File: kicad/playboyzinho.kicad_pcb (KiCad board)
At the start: 2 copper layers, 15 parts, among them SW1 SW_Push, SW2 SW_Push, SW3 SW_Push, SW4 SW_Push, SW5 SW_Push, SW6 SW_Push, SW7 SW_Push, SW8 SW_Push, SW9 SW_SPDT, U1 esp32-s3-pl, U7 (amplificador)_MAX98357_Module

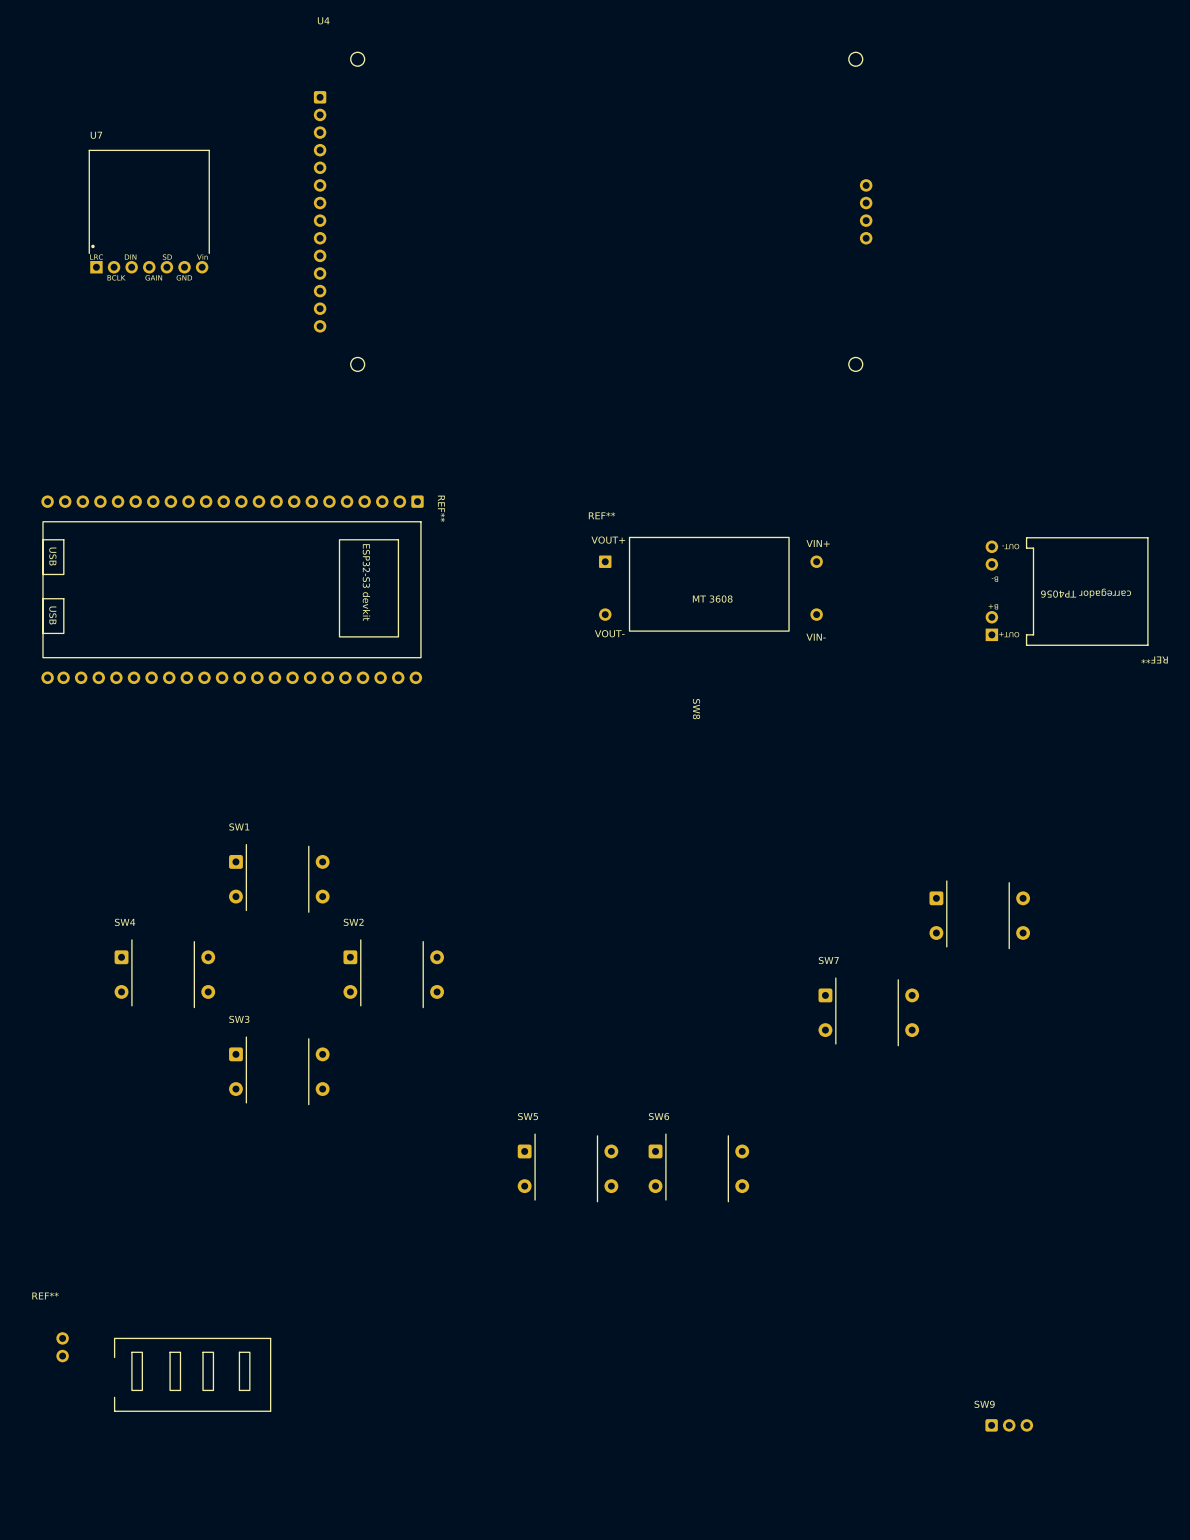
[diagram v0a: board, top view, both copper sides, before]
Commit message: fix: corrige conexões do esquemático e direção dos pinos de determinados símbolos
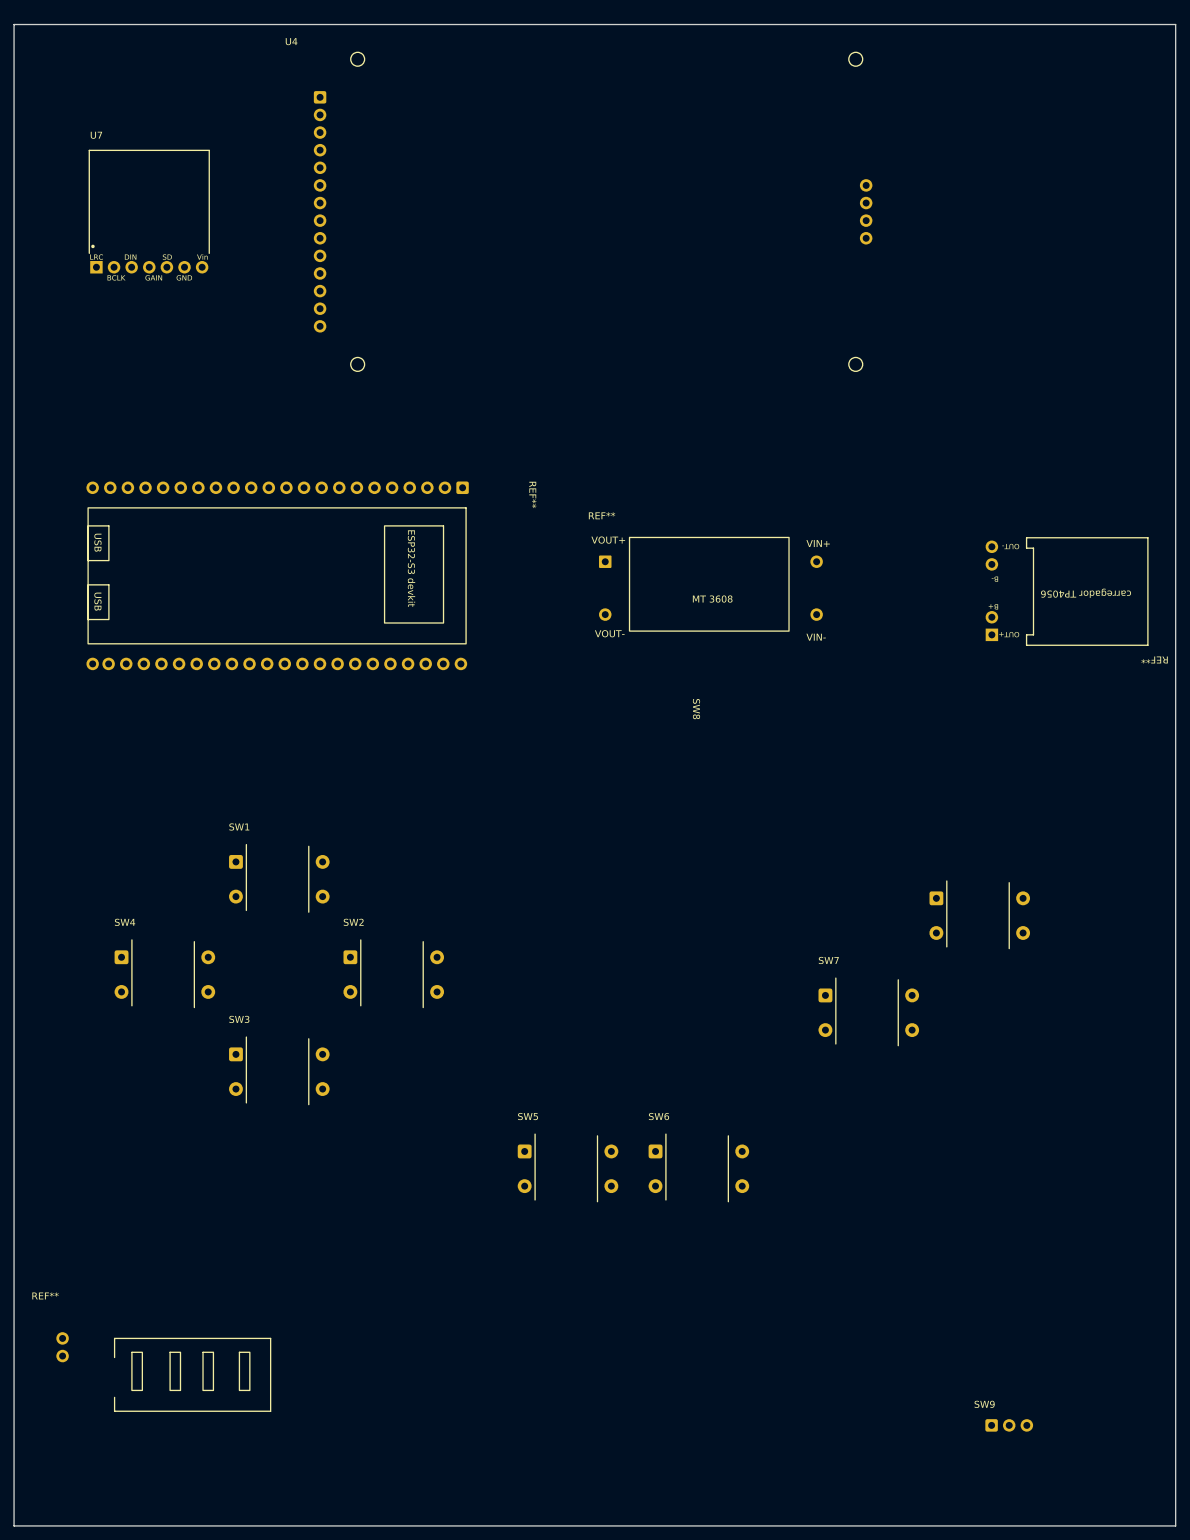
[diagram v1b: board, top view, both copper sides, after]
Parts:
- moved U1 6.80 mm to (-178.8, 40.3)
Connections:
- SW9 pad 1: +BATT -> unconnected-(SW9-A-Pad1)
- SW9 pad 2: -BATT -> Net-(SW9-B)
- SW9 pad 3: unconnected-(SW9-C-Pad3) -> Net-(SW9-C)
- U3 pad 3: +BATT -> Net-(SW9-C)
- U3 pad 4: GND -> Net-(U3-VIN-)
- U4 pad 18: /SD_CS -> /SCK
- U5 pad 1: +5V -> Net-(SW9-B)
- U5 pad 4: GND -> Net-(U3-VIN-)
- U6 pad 1: +BATT -> Net-(SW9-C)
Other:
- board outline added: 167.5 x 216.5 mm
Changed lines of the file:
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@@
 		)
 		(property "Value" "(amplificador)_MAX98357_Module"
-			(at 8.62 4.5 0)
+			(at 7 3.5 0)
 			(unlocked yes)
 			(layer "F.Fab")
@@
 	(footprint "lib-do-playboy:esp32-s3"
 		(layer "F.Cu")
-		(at -185.322001 42.3 -90)
+		(at -178.822001 40.3 -90)
 		(property "Reference" "U1"
 			(at 12.7 23.75 270)
@@
 		)
 		(fp_text user "REF**"
-			(at -1 -2.822001 270)
+			(at -1 -9.5 270)
 			(unlocked yes)
 			(layer "F.SilkS")
@@
 			(layers "*.Cu" "*.Mask")
 			(remove_unused_layers no)
-			(net "+5V")
+			(net "Net-(SW9-B)")
 			(pinfunction "OUT+_1")
-			(pintype "passive")
+			(pintype "power_out")
 		)
 		(pad "2" thru_hole circle
@@
 			(layers "*.Cu" "*.Mask")
 			(remove_unused_layers no)
-			(net "GND")
+			(net "Net-(U3-VIN-)")
 			(pinfunction "OUT-_4")
-			(pintype "passive")
+			(pintype "power_out")
 			(thermal_bridge_angle 90)
 		)
@@
 			(layers "*.Cu" "*.Mask")
 			(remove_unused_layers no)
-			(net "+BATT")
+			(net "Net-(SW9-C)")
 			(pinfunction "VIN+_3")
 			(pintype "power_in")
@@
 			(layers "*.Cu" "*.Mask")
 			(remove_unused_layers no)
-			(net "GND")
+			(net "Net-(U3-VIN-)")
 			(pinfunction "VIN-_4")
 			(pintype "power_in")
@@
 			(layers "*.Cu" "*.Mask")
 			(remove_unused_layers no)
-			(net "+BATT")
+			(net "Net-(SW9-C)")
 			(pinfunction "BAT+_1")
 			(pintype "power_in")
@@
 			(remove_unused_layers no)
 			(roundrect_rratio 0.15)
-			(net "+BATT")
+			(net "unconnected-(SW9-A-Pad1)")
 			(pinfunction "A_1")
-			(pintype "passive")
+			(pintype "passive+no_connect")
 		)
 		(pad "2" thru_hole circle
@@
 			(layers "*.Cu" "*.Mask")
 			(remove_unused_layers no)
-			(net "-BATT")
+			(net "Net-(SW9-B)")
 			(pinfunction "B_2")
 			(pintype "passive")
@@
 			(layers "*.Cu" "*.Mask")
 			(remove_unused_layers no)
-			(net "unconnected-(SW9-C-Pad3)")
+			(net "Net-(SW9-C)")
 			(pinfunction "C_3")
-			(pintype "passive+no_connect")
+			(pintype "passive")
 		)
 		(embedded_fonts no)
@@
 		(at -199.37 -16)
 		(property "Reference" "U4"
-			(at 0.5 -11 0)
+			(at -4.13 -8 0)
 			(unlocked yes)
 			(layer "F.SilkS")
@@
 			(layers "*.Cu" "*.Mask")
 			(remove_unused_layers no)
-			(net "/SD_CS")
+			(net "/SCK")
 			(pinfunction "SD_SCK_18")
 			(pintype "input")
@@
 		(embedded_fonts no)
 	)
+	(gr_rect
+		(start -243.5 -26.5)
+		(end -76 190)
+		(stroke
+			(width 0.05)
+			(type default)
+		)
+		(fill no)
+		(layer "Edge.Cuts")
+	)
 	(embedded_fonts no)

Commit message: feat: finaliza pcb
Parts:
- added U2: ~, lib-do-playboy:bateria, F.Cu at (70.4, 115.0)
- moved SW7 227.4 mm to (-2.50, 137.2)
- moved SW6 224.4 mm to (10.9, 124.5)
- moved SW8 224.2 mm to (10.9, 150.2)
- moved U6 221.8 mm to (-17.4, 197.2)
- moved SW5 221.3 mm to (24.4, 137.5)
- moved U7 215.0 mm to (-17.8, 30.5)
- moved SW9 214.8 mm to (109.8, 207.5)
- moved U1 212.7 mm to (33.0, 59.0)
- moved U4 211.0 mm to (10.0, 10.0)
- moved U3 209.8 mm to (51.0, 66.0)
- moved SW3 204.0 mm to (50.1, 170.2)
- moved SW4 204.0 mm to (31.2, 170.2)
- moved U5 200.1 mm to (97.0, 77.0)
- moved SW2 195.6 mm to (66.6, 144.5)
- moved SW1 193.9 mm to (80.9, 131.0)
- renumbered SW8 to SW1, SW7 to SW2, SW6 to SW3, SW5 to SW4, SW2 to SW5, SW1 to SW6, SW4 to SW7, SW3 to SW8
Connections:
- SW1 pad 1: /Button-8 -> /Button-1
- SW2 pad 1: /Button-7 -> /Button-2
- SW3 pad 1: /Button-6 -> /Button-3
- SW4 pad 1: /Button-5 -> /Button-4
- SW5 pad 1: /Button-2 -> /Button-5
- SW6 pad 1: /Button-1 -> /Button-6
- SW7 pad 1: /Button-4 -> /Button-7
- SW8 pad 1: /Button-3 -> /Button-8
- U1 pad 1: /LED -> /3V3
- U1 pad 10: /Button-3 -> /SCK
- U1 pad 11: /Button-4 -> unconnected-(U1-GPIO18-Pad11)
- U1 pad 12: /RESET -> /MOSI
- U1 pad 16: /CS -> /RESET
- U1 pad 17: /MOSI -> /CS
- U1 pad 18: /SCK -> /DIN
- U1 pad 19: /MISO -> /BCLK
- U1 pad 20: /SD_CS -> /LRC
- U1 pad 23: unconnected-(U1-GND-Pad23) -> GND
- U1 pad 26: /Button-5 -> unconnected-(U1-GPIO1-Pad26)
- U1 pad 27: /Button-6 -> unconnected-(U1-GPIO2-Pad27)
- U1 pad 28: unconnected-(U1-GPIO42-Pad28) -> /Button-1
- U1 pad 29: unconnected-(U1-GPIO41-Pad29) -> /Button-2
- U1 pad 30: unconnected-(U1-GPIO40-Pad30) -> /Button-3
- U1 pad 31: unconnected-(U1-GPIO39-Pad31) -> /Button-5
- U1 pad 32: unconnected-(U1-GPIO38-Pad32) -> /Button-4
- U1 pad 38: unconnected-(U1-GPIO48-Pad38) -> /Button-6
- U1 pad 39: unconnected-(U1-GPIO47-Pad39) -> /Button-8
- U1 pad 4: /LRC -> /SD_CS
- U1 pad 40: /Button-8 -> /Button-7
- U1 pad 43: unconnected-(U1-GND-Pad43) -> GND
- U1 pad 44: unconnected-(U1-GND-Pad44) -> GND
- U1 pad 5: /BCLK -> unconnected-(U1-GPIO5-Pad5)
- U1 pad 6: /DIN -> unconnected-(U1-GPIO6-Pad6)
- U1 pad 7: /Button-7 -> unconnected-(U1-GPIO7-Pad7)
- U1 pad 8: /Button-1 -> unconnected-(U1-GPIO15-Pad8)
- U1 pad 9: /Button-2 -> /MISO
- U3 pad 4: Net-(U3-VIN-) -> GND
- U4 pad 1: unconnected-(U4-T_IRQ-Pad1) -> +5V
- U4 pad 10: /DC -> unconnected-(U4-T_CLK-Pad10)
- U4 pad 11: /RESET -> unconnected-(U4-T_CS-Pad11)
- U4 pad 12: /CS -> unconnected-(U4-T_DIN-Pad12)
- U4 pad 13: GND -> unconnected-(U4-T_DO-Pad13)
- U4 pad 14: +5V -> unconnected-(U4-T_IRQ-Pad14)
- U4 pad 2: unconnected-(U4-T_DO-Pad2) -> GND
- U4 pad 3: unconnected-(U4-T_DIN-Pad3) -> /CS
- U4 pad 4: unconnected-(U4-T_CS-Pad4) -> /RESET
- U4 pad 5: unconnected-(U4-T_CLK-Pad5) -> /DC
- U4 pad 6: /MISO -> /MOSI
- U4 pad 7: /LED -> /SCK
- U4 pad 8: /SCK -> /3V3
- U4 pad 9: /MOSI -> /MISO
- U5 pad 4: Net-(U3-VIN-) -> GND
- U6 pad 2: -BATT -> GND
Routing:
- net Net-(SW9-C): track 0.00 -> 284.2 mm
- net Net-(SW9-B): track 0.00 -> 136.9 mm
- net +5V: track 0.00 -> 133.5 mm
- net /MOSI: track 0.00 -> 119.5 mm
- net /SCK: track 0.00 -> 118.1 mm
- net /MISO: track 0.00 -> 112.6 mm, vias 0 -> 1
- net /Button-3: track 0.00 -> 110.1 mm
- net /Button-4: track 0.00 -> 100.3 mm
- net /SD_CS: track 0.00 -> 87.8 mm
- net /Button-2: track 0.00 -> 85.4 mm
- net /Button-1: track 0.00 -> 85.1 mm
- net +BATT: track 0.00 -> 80.3 mm
- net /Button-8: track 0.00 -> 78.6 mm
- net -BATT: track 0.00 -> 77.5 mm
- net /Button-5: track 0.00 -> 63.0 mm
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- added copper zone on B.Cu, net GND
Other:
- board size 167.5 x 216.5 mm -> 143.2 x 213 mm
